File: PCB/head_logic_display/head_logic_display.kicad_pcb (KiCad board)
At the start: 2 copper layers, 48 x 21.6 mm, 73 parts, among them J1 Conn_01x03_Socket, J2 Conn_01x03_Socket

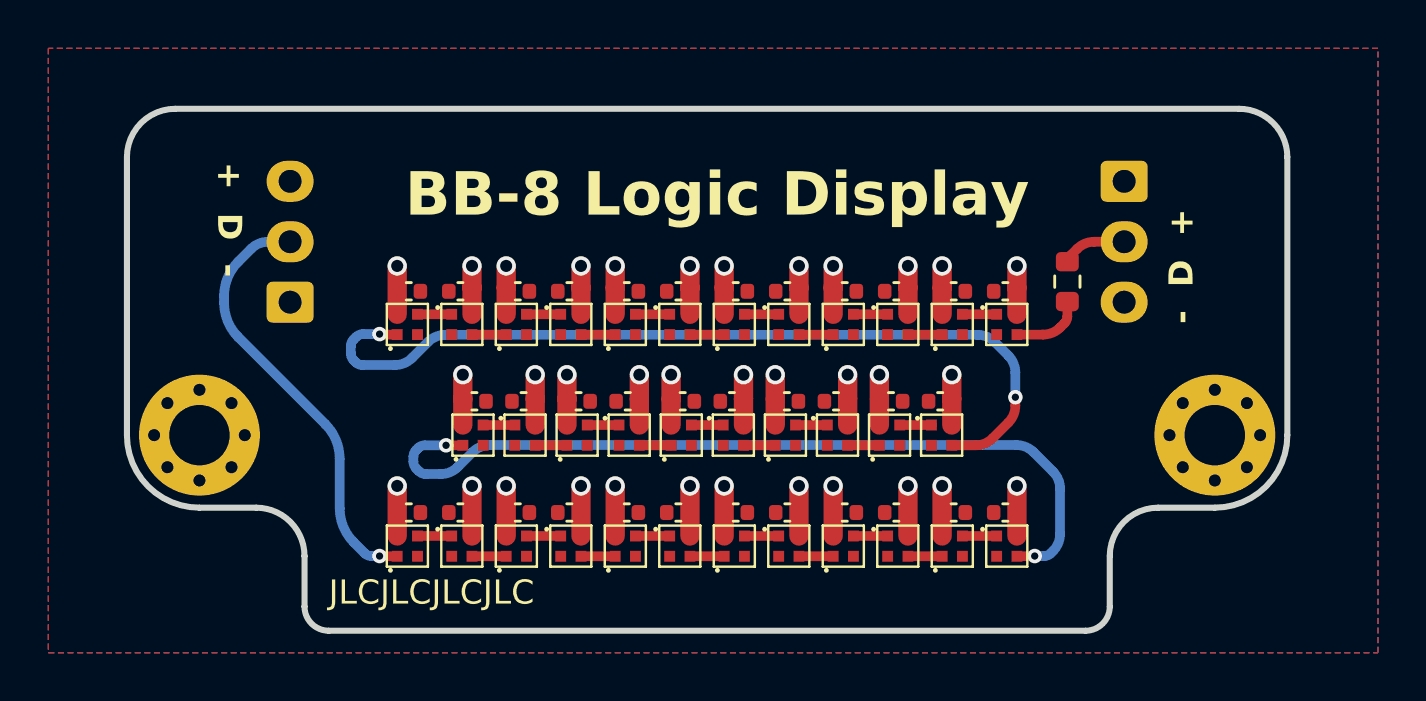
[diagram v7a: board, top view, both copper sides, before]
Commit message: Fix logic lens led rotation
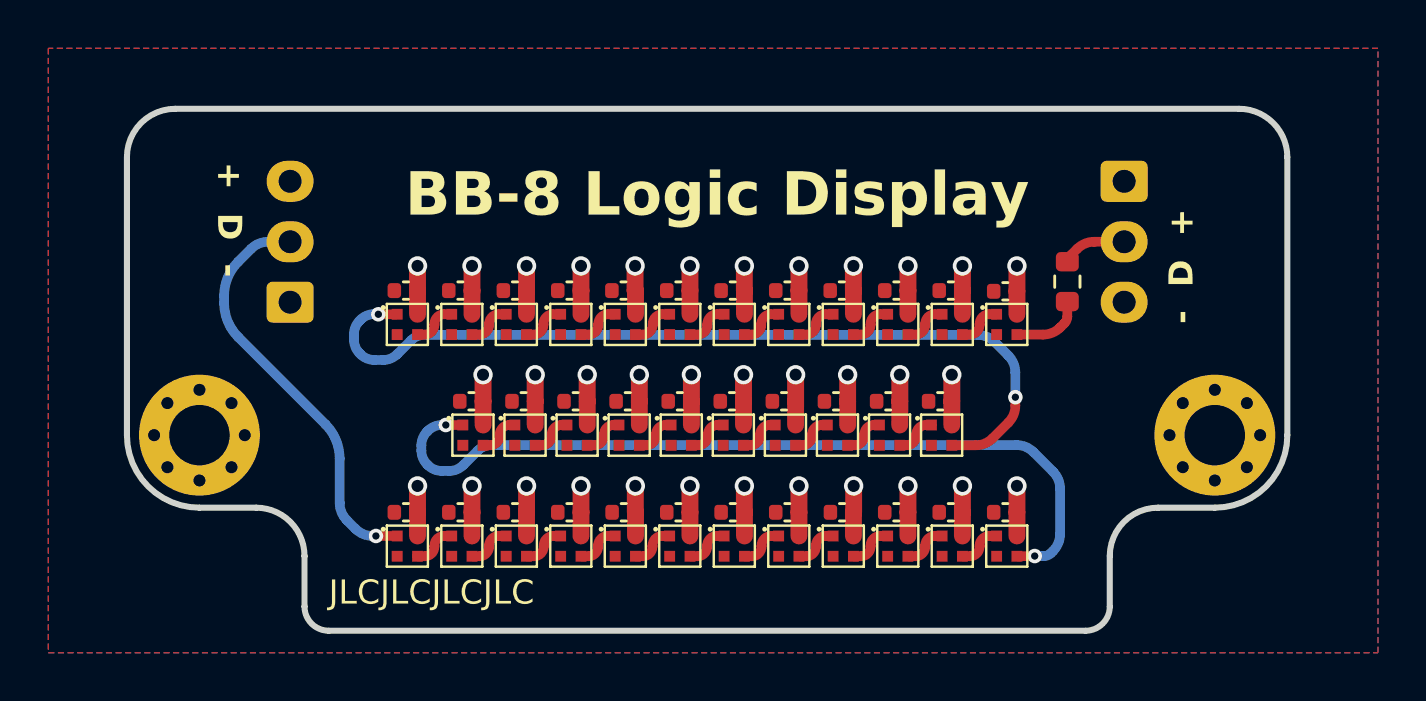
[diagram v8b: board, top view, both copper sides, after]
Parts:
- moved C8 0.14 mm to (87.8, 91.0), turned to 180 degrees
- moved C6 0.13 mm to (92.3, 91.0), turned to 180 degrees
- moved C30 0.13 mm to (87.8, 100.2), turned to 180 degrees
- moved C4 0.13 mm to (96.8, 91.0), turned to 180 degrees
- moved C28 0.12 mm to (92.3, 100.2), turned to 180 degrees
- moved C22 0.12 mm to (81.5, 95.6), turned to 180 degrees
- moved C2 0.12 mm to (101.3, 91.0), turned to 180 degrees
- moved C12 0.12 mm to (78.8, 91.0), turned to 180 degrees
- moved C20 0.12 mm to (85.8, 95.6), turned to 180 degrees
- moved C10 0.12 mm to (83.3, 91.0), turned to 180 degrees
- moved C24 0.12 mm to (101.3, 100.2), turned to 180 degrees
- moved C34 0.12 mm to (78.8, 100.2), turned to 180 degrees
- moved C18 0.12 mm to (90.1, 95.6), turned to 180 degrees
- moved C32 0.12 mm to (83.3, 100.2), turned to 180 degrees
- moved C16 0.12 mm to (94.4, 95.6), turned to 180 degrees
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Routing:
- net /DATA_OUT: track 18.5 -> 17.8 mm
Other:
- board text added: "Rev 1.1"
- board text removed: "Rev 1.0"
